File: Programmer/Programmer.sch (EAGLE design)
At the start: 70 parts, among them Q1 16Mhz, SW1 SWITCHMJTP1234, U1 MIC5205-3.3YM5 TR, U2 ATMEGA32U4TQFP, U3 USBFCI-MICROB

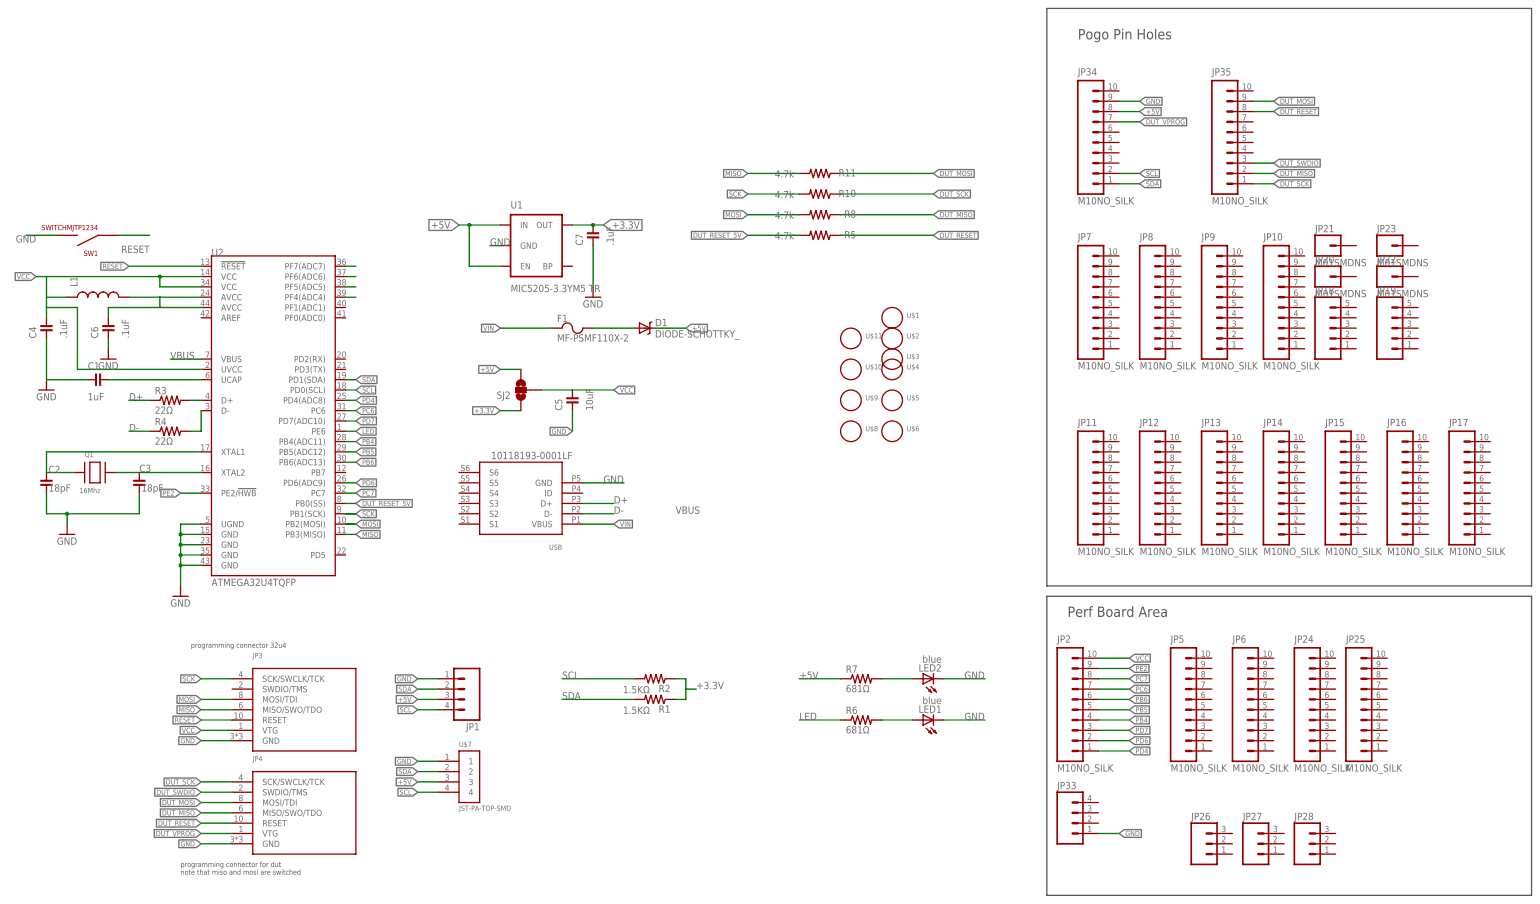
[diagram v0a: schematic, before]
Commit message: Check point of current PCB designs. Among other things I think this change includes rewiring of programming lines on many of the boards,.
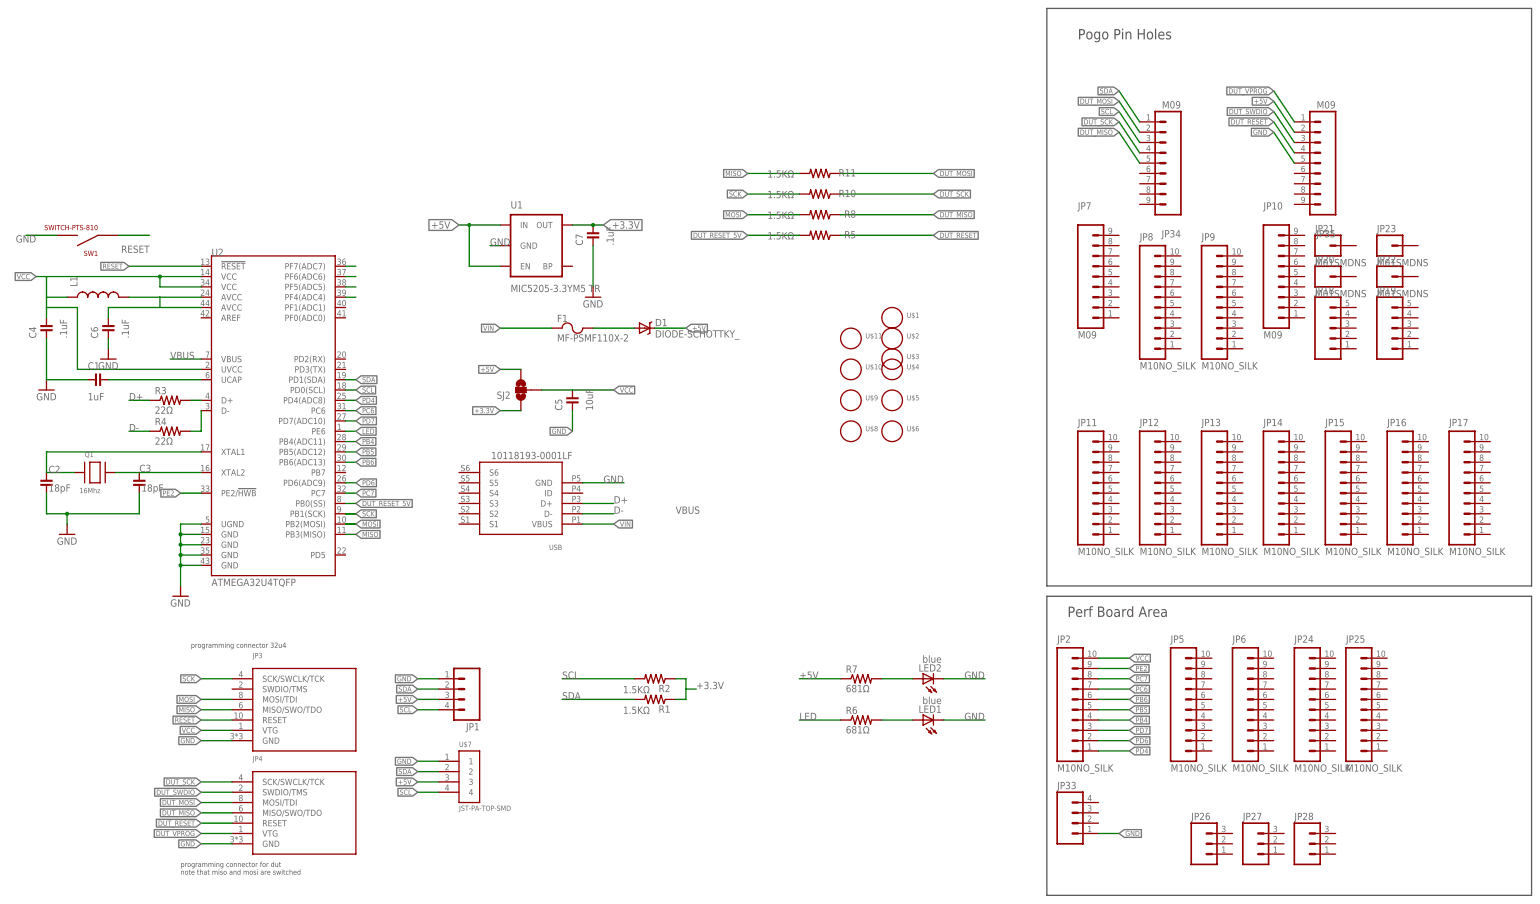
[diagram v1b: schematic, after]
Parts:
- JP10, JP34, JP35, JP7: value M10NO_SILK -> M09; device SparkFun-Connectors:M10NO_SILK -> SparkFun-Connectors:M09
- R10, R11, R5, R8: value 4.7k -> 1.5KΩ
- SW1: value SWITCHMJTP1234 -> SWITCH-PTS-810; device Modulo:SWITCHMJTP1234 -> Modulo:SWITCH-PTS-810
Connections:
- net +5V: now also JP35.2; no longer JP34.8
- net DUT_MISO: now also JP34.5; no longer JP35.2
- net DUT_MOSI: now also JP34.2; no longer JP35.9
- net DUT_RESET: now also JP35.4; no longer JP35.8
- net DUT_SCK: now also JP34.4; no longer JP35.1
- net DUT_VPROG: now also JP35.1; no longer JP34.7
- net GND: now also JP35.5; no longer JP34.9
- net SCL: now also JP34.3; no longer JP34.2
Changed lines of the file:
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@@
 <part name="U$3" library="Modulo" deviceset="HOLE" device="#2"/>
 <part name="U$4" library="Modulo" deviceset="HOLE" device="#2"/>
-<part name="JP7" library="SparkFun-Connectors" deviceset="M10" device="NO_SILK"/>
+<part name="JP7" library="SparkFun-Connectors" deviceset="M09" device=""/>
 <part name="JP8" library="SparkFun-Connectors" deviceset="M10" device="NO_SILK"/>
 <part name="JP9" library="SparkFun-Connectors" deviceset="M10" device="NO_SILK"/>
-<part name="JP10" library="SparkFun-Connectors" deviceset="M10" device="NO_SILK"/>
+<part name="JP10" library="SparkFun-Connectors" deviceset="M09" device=""/>
 <part name="JP11" library="SparkFun-Connectors" deviceset="M10" device="NO_SILK"/>
 <part name="JP12" library="SparkFun-Connectors" deviceset="M10" device="NO_SILK"/>
@@
 <part name="R1" library="Modulo" deviceset="RESISTOR" device="-1.5KΩ" value="1.5KΩ"/>
 <part name="R2" library="Modulo" deviceset="RESISTOR" device="-1.5KΩ" value="1.5KΩ"/>
-<part name="SW1" library="Modulo" deviceset="SWITCH" device="MJTP1234" value="SWITCHMJTP1234"/>
+<part name="SW1" library="Modulo" deviceset="SWITCH" device="-PTS-810" value="SWITCH-PTS-810"/>
 <part name="F1" library="Modulo" deviceset="FUSE" device="" value="MF-PSMF110X-2">
 <attribute name="PARTNUM" value="MF-PSFM110X-2"/>
@@
 <part name="C7" library="Modulo" deviceset="CAPACITOR" device="-.1UF" value=".1uF"/>
 <part name="GND2" library="SparkFun-Aesthetics" deviceset="GND" device=""/>
-<part name="R8" library="Modulo" deviceset="RESISTOR" device="-1.5KΩ" value="4.7k"/>
-<part name="R10" library="Modulo" deviceset="RESISTOR" device="-1.5KΩ" value="4.7k"/>
-<part name="R11" library="Modulo" deviceset="RESISTOR" device="-1.5KΩ" value="4.7k"/>
+<part name="R8" library="Modulo" deviceset="RESISTOR" device="-1.5KΩ" value="1.5KΩ"/>
+<part name="R10" library="Modulo" deviceset="RESISTOR" device="-1.5KΩ" value="1.5KΩ"/>
+<part name="R11" library="Modulo" deviceset="RESISTOR" device="-1.5KΩ" value="1.5KΩ"/>
 <part name="D1" library="SparkFun-DiscreteSemi" deviceset="DIODE-SCHOTTKY" device="_"/>
 <part name="U$7" library="Modulo" deviceset="JST-PA" device="-TOP-SMD"/>
@@
 <part name="JP2" library="SparkFun-Connectors" deviceset="M10" device="NO_SILK"/>
 <part name="SJ2" library="SparkFun-Passives" deviceset="SOLDERJUMPER_2WAY" device="PASTE1&amp;2"/>
-<part name="R5" library="Modulo" deviceset="RESISTOR" device="-1.5KΩ" value="4.7k"/>
+<part name="R5" library="Modulo" deviceset="RESISTOR" device="-1.5KΩ" value="1.5KΩ"/>
 <part name="JP3" library="Modulo" deviceset="ICSP" device=""/>
 <part name="JP4" library="Modulo" deviceset="ICSP" device=""/>
@@
 <part name="JP25" library="SparkFun-Connectors" deviceset="M10" device="NO_SILK"/>
 <part name="JP33" library="SparkFun-Connectors" deviceset="M04" device="1X04_NO_SILK"/>
-<part name="JP34" library="SparkFun-Connectors" deviceset="M10" device="NO_SILK"/>
-<part name="JP35" library="SparkFun-Connectors" deviceset="M10" device="NO_SILK"/>
+<part name="JP34" library="SparkFun-Connectors" deviceset="M09" device=""/>
+<part name="JP35" library="SparkFun-Connectors" deviceset="M09" device=""/>
 <part name="JP26" library="SparkFun-Connectors" deviceset="M03" device="1X03_NO_SILK"/>
 <part name="JP27" library="SparkFun-Connectors" deviceset="M03" device="1X03_NO_SILK"/>
@@
 <instance part="JP25" gate="G$1" x="619.76" y="86.36"/>
 <instance part="JP33" gate="G$1" x="553.72" y="50.8"/>
-<instance part="JP34" gate="G$1" x="553.72" y="226.06"/>
-<instance part="JP35" gate="G$1" x="586.74" y="226.06"/>
+<instance part="JP34" gate="G$1" x="579.12" y="213.36" rot="R180"/>
+<instance part="JP35" gate="G$1" x="617.22" y="213.36" rot="R180"/>
 <instance part="JP26" gate="G$1" x="584.2" y="45.72"/>
 <instance part="JP27" gate="G$1" x="596.9" y="45.72"/>
@@
 </segment>
 <segment>
-<pinref part="JP34" gate="G$1" pin="9"/>
-<wire x1="563.88" y1="228.6" x2="568.96" y2="228.6" width="0.1524" layer="91"/>
-<label x="568.96" y="228.6" size="1.27" layer="95" xref="yes"/>
-</segment>
-<segment>
 <pinref part="C6" gate="G$1" pin="2"/>
 <wire x1="314.96" y1="170.18" x2="314.96" y2="167.64" width="0.1524" layer="91"/>
 <pinref part="GND4" gate="1" pin="GND"/>
+</segment>
+<segment>
+<pinref part="JP35" gate="G$1" pin="5"/>
+<wire x1="607.06" y1="213.36" x2="601.98" y2="220.98" width="0.1524" layer="91"/>
+<label x="601.98" y="220.98" size="1.27" layer="95" rot="R180" xref="yes"/>
 </segment>
 </net>
@@
 </segment>
 <segment>
-<pinref part="JP34" gate="G$1" pin="2"/>
-<wire x1="563.88" y1="210.82" x2="568.96" y2="210.82" width="0.1524" layer="91"/>
-<label x="568.96" y="210.82" size="1.27" layer="95" xref="yes"/>
+<pinref part="JP34" gate="G$1" pin="3"/>
+<wire x1="568.96" y1="218.44" x2="563.88" y2="226.06" width="0.1524" layer="91"/>
+<label x="563.88" y="226.06" size="1.27" layer="95" rot="R180" xref="yes"/>
 </segment>
 </net>
@@
 <segment>
 <pinref part="JP34" gate="G$1" pin="1"/>
-<wire x1="563.88" y1="208.28" x2="568.96" y2="208.28" width="0.1524" layer="91"/>
-<label x="568.96" y="208.28" size="1.27" layer="95" xref="yes"/>
+<wire x1="568.96" y1="223.52" x2="563.88" y2="231.14" width="0.1524" layer="91"/>
+<label x="563.88" y="231.14" size="1.27" layer="95" rot="R180" xref="yes"/>
 </segment>
 </net>
@@
 </segment>
 <segment>
-<pinref part="JP35" gate="G$1" pin="8"/>
-<wire x1="596.9" y1="226.06" x2="601.98" y2="226.06" width="0.1524" layer="91"/>
-<label x="601.98" y="226.06" size="1.27" layer="95" xref="yes"/>
+<pinref part="JP35" gate="G$1" pin="4"/>
+<wire x1="607.06" y1="215.9" x2="601.98" y2="223.52" width="0.1524" layer="91"/>
+<label x="601.98" y="223.52" size="1.27" layer="95" rot="R180" xref="yes"/>
 </segment>
 </net>
@@
 </segment>
 <segment>
-<pinref part="JP35" gate="G$1" pin="9"/>
-<wire x1="596.9" y1="228.6" x2="601.98" y2="228.6" width="0.1524" layer="91"/>
-<label x="601.98" y="228.6" size="1.27" layer="95" xref="yes"/>
+<pinref part="JP34" gate="G$1" pin="2"/>
+<wire x1="568.96" y1="220.98" x2="563.88" y2="228.6" width="0.1524" layer="91"/>
+<label x="563.88" y="228.6" size="1.27" layer="95" rot="R180" xref="yes"/>
 </segment>
 </net>
@@
 </segment>
 <segment>
-<pinref part="JP35" gate="G$1" pin="1"/>
-<wire x1="596.9" y1="208.28" x2="601.98" y2="208.28" width="0.1524" layer="91"/>
-<label x="601.98" y="208.28" size="1.27" layer="95" xref="yes"/>
+<pinref part="JP34" gate="G$1" pin="4"/>
+<wire x1="568.96" y1="215.9" x2="563.88" y2="223.52" width="0.1524" layer="91"/>
+<label x="563.88" y="223.52" size="1.27" layer="95" rot="R180" xref="yes"/>
 </segment>
 </net>
@@
 </segment>
 <segment>
-<pinref part="JP35" gate="G$1" pin="2"/>
-<wire x1="596.9" y1="210.82" x2="601.98" y2="210.82" width="0.1524" layer="91"/>
-<label x="601.98" y="210.82" size="1.27" layer="95" xref="yes"/>
+<pinref part="JP34" gate="G$1" pin="5"/>
+<wire x1="568.96" y1="213.36" x2="563.88" y2="220.98" width="0.1524" layer="91"/>
+<label x="563.88" y="220.98" size="1.27" layer="95" rot="R180" xref="yes"/>
 </segment>
 </net>
@@
 </segment>
 <segment>
-<pinref part="JP34" gate="G$1" pin="7"/>
-<wire x1="563.88" y1="223.52" x2="568.96" y2="223.52" width="0.1524" layer="91"/>
-<label x="568.96" y="223.52" size="1.27" layer="95" xref="yes"/>
+<pinref part="JP35" gate="G$1" pin="1"/>
+<wire x1="607.06" y1="223.52" x2="601.98" y2="231.14" width="0.1524" layer="91"/>
+<label x="601.98" y="231.14" size="1.27" layer="95" rot="R180" xref="yes"/>
 </segment>
 </net>
@@
 </segment>
 <segment>
-<pinref part="JP34" gate="G$1" pin="8"/>
-<wire x1="563.88" y1="226.06" x2="568.96" y2="226.06" width="0.1524" layer="91"/>
-<label x="568.96" y="226.06" size="1.27" layer="95" xref="yes"/>
+<pinref part="JP35" gate="G$1" pin="2"/>
+<wire x1="607.06" y1="220.98" x2="601.98" y2="228.6" width="0.1524" layer="91"/>
+<label x="601.98" y="228.6" size="1.27" layer="95" rot="R180" xref="yes"/>
 </segment>
 </net>
@@
 <segment>
 <pinref part="JP35" gate="G$1" pin="3"/>
-<wire x1="596.9" y1="213.36" x2="601.98" y2="213.36" width="0.1524" layer="91"/>
-<label x="601.98" y="213.36" size="1.27" layer="95" xref="yes"/>
-</segment>
-</net>
+<wire x1="607.06" y1="218.44" x2="601.98" y2="226.06" width="0.1524" layer="91"/>
+<label x="601.98" y="226.06" size="1.27" layer="95" rot="R180" xref="yes"/>
+</segment>
+</net>
